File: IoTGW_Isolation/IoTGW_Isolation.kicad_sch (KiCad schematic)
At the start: 17 parts, among them U1 74LVC2G14, U2 HCPL-0600, U3 TLE2426xD, U4 VO2630, U5 TEA1-0505, U6 ISO1452BDWR, U7 PC817, U8 PC817

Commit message: reverse pol prot
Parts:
- added Q?: PMOS, symbol Simulation_SPICE:PMOS
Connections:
- net +5V_OUT: now also Q?.1 (D); no longer C3.1, C5.1, U6.16 (VCC2)
- net GND_OUT: now also Q?.2 (G)
- new net: C3.1, C5.1, U6.16 (VCC2)
- new net +5V_PROT: Q?.3 (S)
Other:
- note added: "choose a pmos will it be ok to use it with rs-485 isolater make a simulation in falstad"

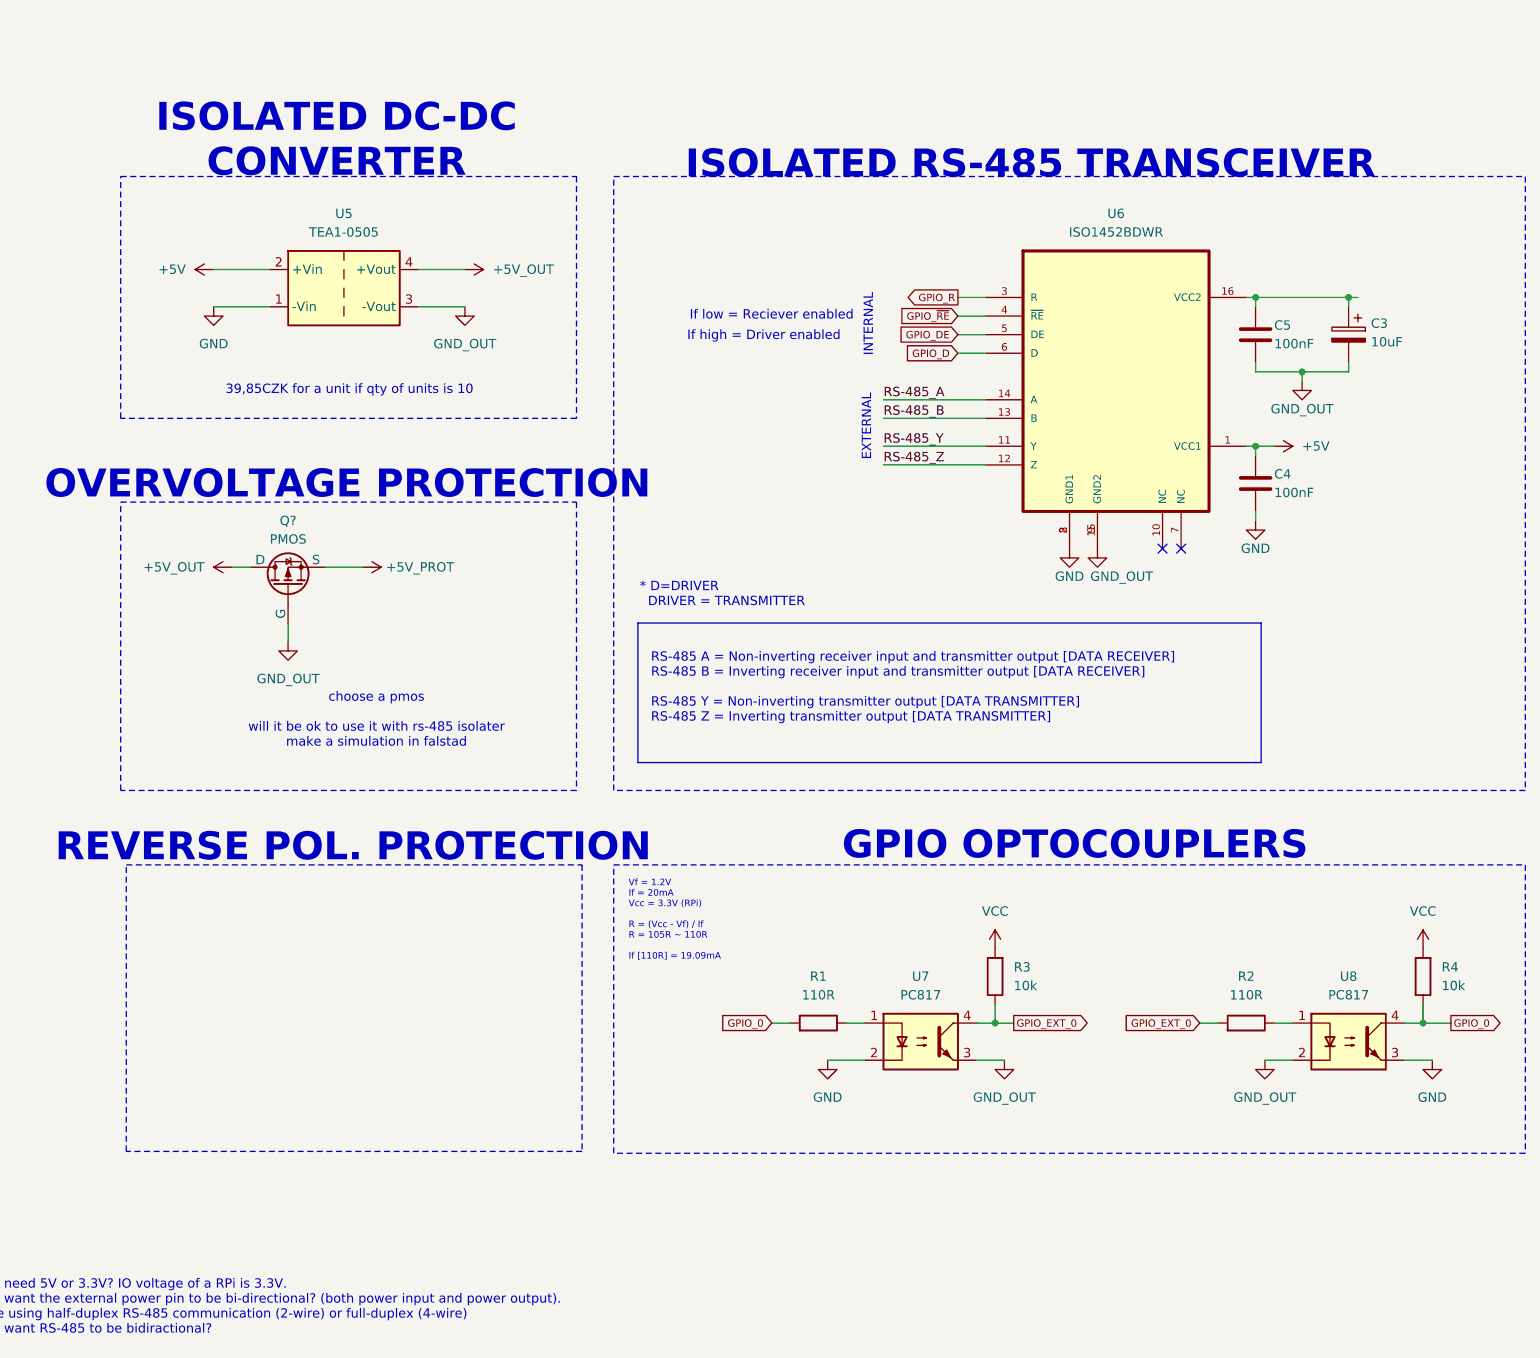
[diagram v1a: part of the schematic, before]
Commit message: updated schematic - comp cost
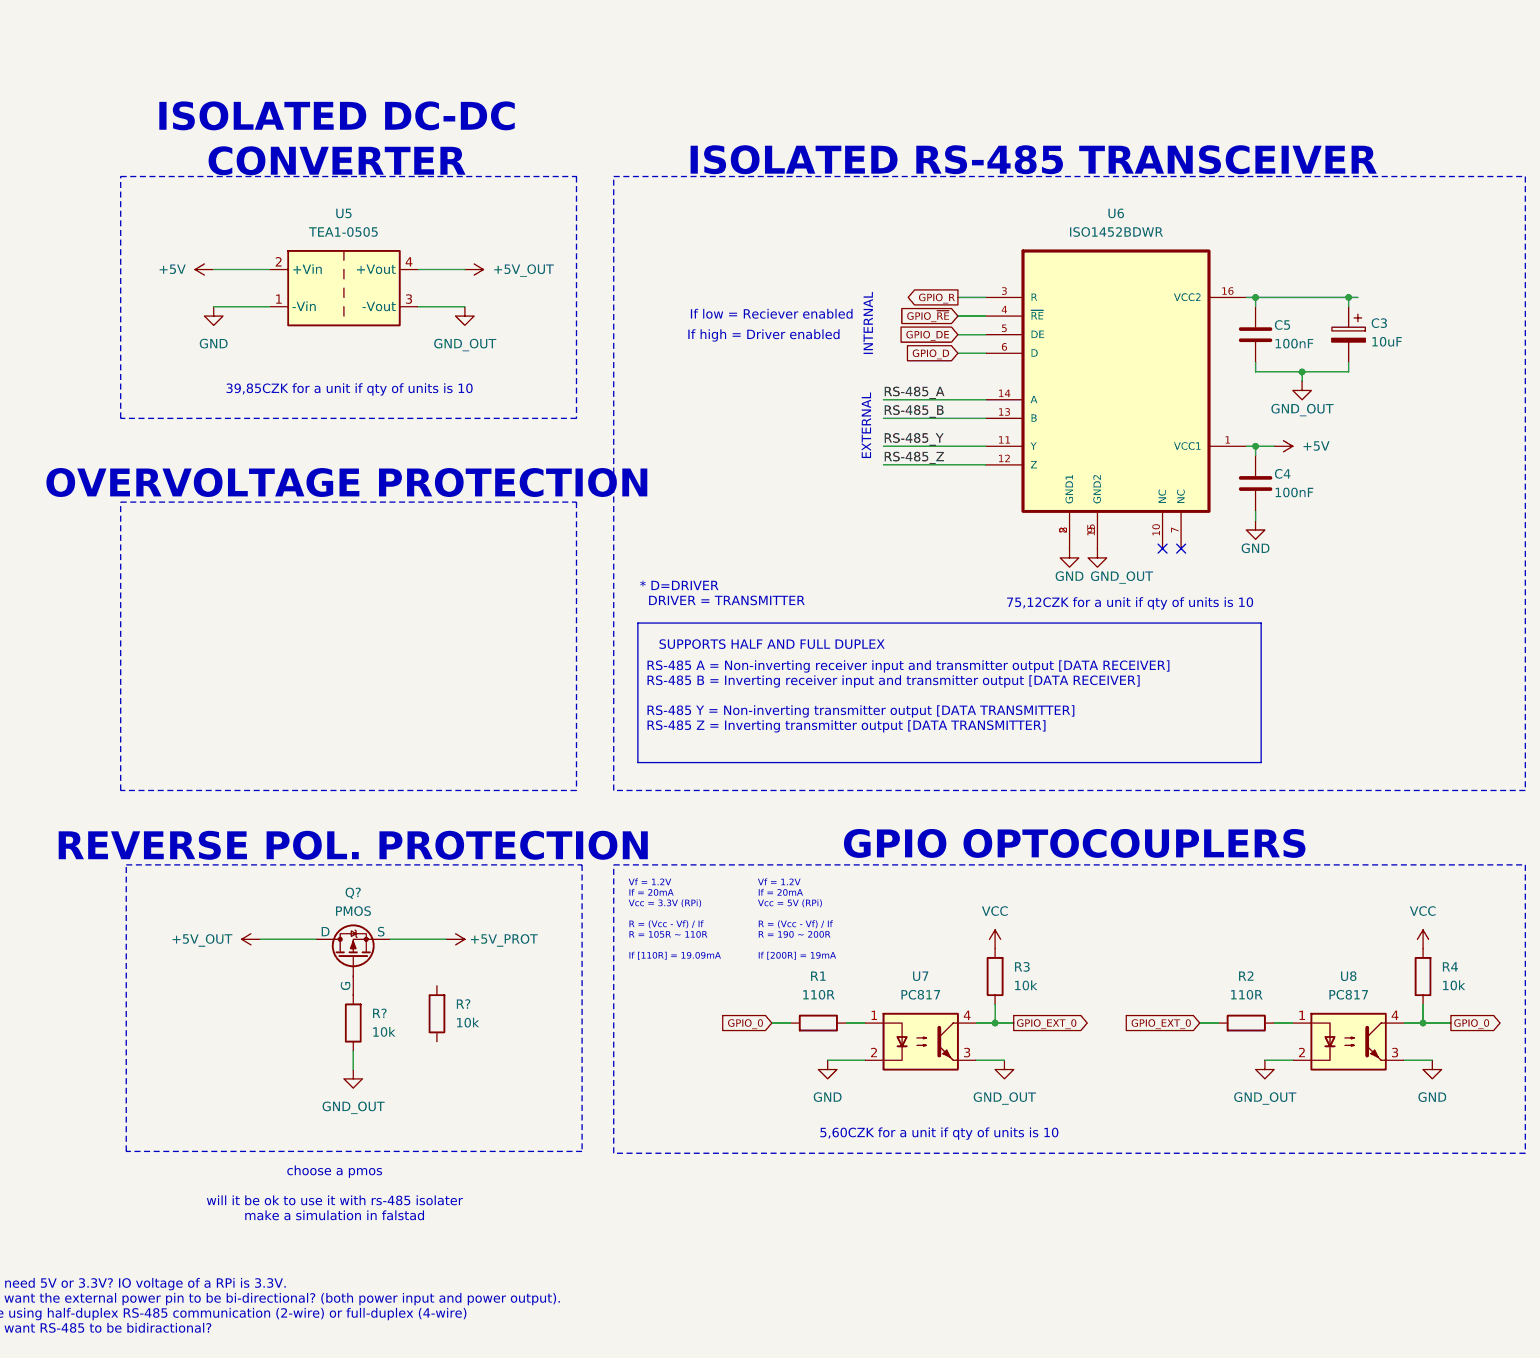
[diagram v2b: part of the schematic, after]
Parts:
- removed Q?: PMOS, symbol Simulation_SPICE:PMOS
- added Q?: PMOS, symbol Simulation_SPICE:PMOS
- added R? (x2): 10k, symbol Device:R
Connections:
- net +5V_OUT: now also Q?.1 (D)
- net +5V_PROT: now also Q?.3 (S)
- net GND_OUT: now also R?.1
- new net: Q?.2 (G), R?.2
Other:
- note added: "5,60CZK for a unit if qty of units is 10"
- note added: "75,12CZK for a unit if qty of units is 10"
- note added: "SUPPORTS HALF AND FULL DUPLEX"
- note added: "Vf = 1.2V If = 20mA Vcc = 5V (RPi) R = (Vcc - Vf) / If R = 190 ~ 200R If [200R] = 19mA"

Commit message: schematic upd
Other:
- note added: "NOT NEEDED SINCE ITS ONLY OUTPUT"
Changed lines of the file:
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@@
+		)
+	)
+	(text "NOT NEEDED SINCE \nITS ONLY OUTPUT"
+		(exclude_from_sim no)
+		(at 77.47 90.805 0)
+		(effects
+			(font
+				(face "Bahnschrift")
+				(size 3 3)
+				(thickness 0.6)
+				(bold yes)
+				(color 0 0 0 1)
+			)
 		)
 	)

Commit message: Schematic update
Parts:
- removed C3: 10uF, symbol Device:C_Polarized
- removed C5: 100nF, symbol Device:C
- removed Q?: PMOS, symbol Simulation_SPICE:PMOS
- removed R? (x2): 10k, symbol Device:R
- removed U6: ISO1452BDWR, ISO1410DWR:SOIC127P1030X265-16N, symbol ISO1410DWR:ISO1452BDWR
- added C3: 100nF, symbol Device:C
- added C5: 10uF, symbol Device:C_Polarized
- added F2: Polyfuse, Fuse:Fuse_0805_2012Metric, symbol Device:Polyfuse
- added H1, H2, H3, H4: M3, symbol Mechanical:MountingHole_Pad
- added J1, J2: JST-XH 2pin, symbol Connector:Conn_01x02_Pin
- added J3: JST-XH 3pin, symbol Connector:Conn_01x03_Pin
- added Q1: Q_PMOS, Package_TO_SOT_SMD:SOT-23-3, symbol Device:Q_PMOS_GSD
- added R1, R10, R12, R14, R8: 10k, symbol Device:R
- added R11, R13, R7, R9: 200R, symbol Device:R
- added R6: 120R, symbol Device:R
- added U10, U11, U12, U9: PC817, Package_DIP:DIP-4_W7.62mm, symbol Isolator:PC817
- added U7: ISO1452BDWR, ISO1410DWR:SOIC127P1030X265-16N, symbol ISO1410DWR:ISO1452BDWR
- R2: renamed from R1; value 110R -> 200R
- R4: renamed from R2; value 110R -> 200R
- renumbered R4 to R5, U7 to U6
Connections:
- net +5V: now also U7.1 (VCC1)
- net +5V_OUT: now also F2.1, Q1.3 (D)
- net +5V_PROT: now also R3.2, R5.2, C3.1, C5.1, Q1.2 (S), R10.2, R12.2, R14.2, R8.2, U7.16 (VCC2)
- net GND: now also U10.3, U11.2, U12.3, U7.2 (GND1), U7.8 (GND1), U9.2
- net GND_OUT: now also C3.2, C5.2, J1.2 (Pin_2), R1.1, U10.2, U11.3, U12.2, U7.15 (GND2), U7.9 (GND2), U9.3
- net GPIO_D: now also U7.6 (D)
- net GPIO_DE: now also U7.5 (DE)
- net GPIO_EXT_0: now also J3.1 (Pin_1)
- net GPIO_R: now also U7.3 (R)
- net GPIO_~{RE}: now also U7.4 (~{RE})
- net RS-485_A: now also J2.1 (Pin_1), R6.2, U7.14 (A)
- net RS-485_B: now also J2.2 (Pin_2), R6.1, U7.13 (B)
- net RS-485_Y: now also U7.11 (Y)
- net RS-485_Z: now also U7.12 (Z)
- net VCC: no longer R3.2, R5.2
- net GPIO_0 renamed GPIO_OPTO_0
- new net: R11.1, U11.1
- new net: Q1.1 (G), R1.2
- new net: R7.1, U9.1
- new net: R13.1, U12.1
- new net: R9.1, U10.1
- new net 5V_CONN: F2.2, J1.1 (Pin_1)
- new net GPIO_EXT_1: J3.2 (Pin_2), R8.1, R9.2, U9.4
- new net GPIO_EXT_2: J3.3 (Pin_3), R12.1, R13.2, U11.4
- new net GPIO_OPTO_1: R10.1, R7.2, U10.4
- new net GPIO_OPTO_2: R11.2, R14.1, U12.4
- no-connect marks 2 -> 8
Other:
- note added: "* D = DRIVER DRIVER = TRANSMITTER"
- note added: "*The unit price is set for an order quantity of 10 units"
- note added: "1. Q: [] 2. Q: [] 3. Q: [] 4. Q: [] 5. Q: []"
- note added: "39,85CZK"
- note added: "5,60CZK"
- note added: "75,12CZK"
- note added: "A zener diode can protect against overvoltage"
- note added: "CIRCUIT PROTECTION"
- note added: "I think we dont need it at all: Cost inneffective."
- note added: "MECHANICAL"
- note added: "SHORT CIRCUIT PROTECTION"
- note added: "low Rds on"
- note removed: "* D=DRIVER DRIVER = TRANSMITTER"
- note removed: "1. Q: Do we need 5V or 3.3V? IO voltage of a RPi is 3.3V. 2. Q: Do we want the external power pin to be bi-directional? (both power input and power output). 3. Q: Are we using half-duplex RS-485 communication (2-wire) or full-duplex (4-wire) 4. Q: Do we want RS-485 to be bidiractional? 5. Q: []"
- note removed: "39,85CZK for a unit if qty of units is 10"
- note removed: "5,60CZK for a unit if qty of units is 10"
- note removed: "75,12CZK for a unit if qty of units is 10"
- note removed: "ISOLATED DC-DC CONVERTER"
- note removed: "NOT NEEDED SINCE ITS ONLY OUTPUT"
- note removed: "OVERVOLTAGE PROTECTION"
- note removed: "choose a pmos will it be ok to use it with rs-485 isolater make a simulation in falstad"
- moved on the sheet: C1, C2, R2, R3, R4, R5, U1A, U1B, U1C, U2, U3, U4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

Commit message: footprints + pcb
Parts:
- removed C1: 220uF, symbol Device:C_Polarized
- removed C2: 1uF, symbol Device:C
- removed J1, J2: JST-XH 2pin, symbol Connector:Conn_01x02_Pin
- removed J3: JST-XH 3pin, symbol Connector:Conn_01x03_Pin
- removed U1: 74LVC2G14, symbol 74xGxx:74LVC2G14
- removed U10, U11, U12, U6, U8, U9: PC817, Package_DIP:DIP-4_W7.62mm, symbol Isolator:PC817
- removed U2: HCPL-0600, Package_SO:SOIC-8_3.9x4.9mm_P1.27mm, symbol Isolator:HCPL-0600
- removed U3: TLE2426xD, Package_SO:SOIC-8_3.9x4.9mm_P1.27mm, symbol Reference_Voltage:TLE2426xD
- removed U4: VO2630, Package_DIP:DIP-8_W7.62mm, symbol Isolator:VO2630
- added J1: Molex 39502-1002, IoTGW:Molex_2pin_3.50, symbol Connector:Conn_01x02_Socket
- added J3: Molex 39502-1007, IoTGW:Molex_7pin_3.50, symbol Connector:Conn_01x07_Socket
- added U3, U4, U5, U6, U7, U8: LTV-817S, Package_DIP:SMDIP-4_W9.53mm, symbol Isolator:LTV-817S
- C1: renamed from C3; footprint (none) -> Capacitor_SMD:C_0805_2012Metric_Pad1.18x1.45mm_HandSolder
- C2: renamed from C4; footprint (none) -> Capacitor_SMD:C_0805_2012Metric_Pad1.18x1.45mm_HandSolder
- C3: renamed from C5; footprint (none) -> Capacitor_Tantalum_SMD:CP_EIA-3216-18_Kemet-A_Pad1.58x1.35mm_HandSolder
- H1, H2, H3, H4: footprint (none) -> MountingHole:MountingHole_3.2mm_M3_Pad_Via
- Q1: footprint Package_TO_SOT_SMD:SOT-23-3 -> (none)
- R10: renamed from R9; footprint (none) -> Resistor_SMD:R_0805_2012Metric_Pad1.20x1.40mm_HandSolder
- R11: renamed from R13; footprint (none) -> Resistor_SMD:R_0805_2012Metric_Pad1.20x1.40mm_HandSolder
- R12: renamed from R5; footprint (none) -> Resistor_SMD:R_0805_2012Metric_Pad1.20x1.40mm_HandSolder
- R13: renamed from R10; footprint (none) -> Resistor_SMD:R_0805_2012Metric_Pad1.20x1.40mm_HandSolder
- R14: footprint (none) -> Resistor_SMD:R_0805_2012Metric_Pad1.20x1.40mm_HandSolder
- R2: renamed from R6; footprint (none) -> Resistor_SMD:R_0805_2012Metric_Pad1.20x1.40mm_HandSolder
- R3: renamed from R2; footprint (none) -> Resistor_SMD:R_0805_2012Metric_Pad1.20x1.40mm_HandSolder
- R4: renamed from R7; footprint (none) -> Resistor_SMD:R_0805_2012Metric_Pad1.20x1.40mm_HandSolder
- R5: renamed from R11; footprint (none) -> Resistor_SMD:R_0805_2012Metric_Pad1.20x1.40mm_HandSolder
- R6: renamed from R3; footprint (none) -> Resistor_SMD:R_0805_2012Metric_Pad1.20x1.40mm_HandSolder
- R7: renamed from R8; footprint (none) -> Resistor_SMD:R_0805_2012Metric_Pad1.20x1.40mm_HandSolder
- R8: renamed from R12; footprint (none) -> Resistor_SMD:R_0805_2012Metric_Pad1.20x1.40mm_HandSolder
- R9: renamed from R4; footprint (none) -> Resistor_SMD:R_0805_2012Metric_Pad1.20x1.40mm_HandSolder
- U2: renamed from U7; footprint ISO1410DWR:SOIC127P1030X265-16N -> Package_SO:SOIC-16W_7.5x10.3mm_P1.27mm
- renumbered F2 to F1, U5 to U1
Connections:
- net +5V: now also J1.2 (Pin_2)
- net 5V_CONN: now also J3.2 (Pin_2)
- net GND: now also J1.1 (Pin_1), U3.2, U4.2, U5.2, U6.3, U7.3, U8.3
- net GND_OUT: now also J3.1 (Pin_1), U3.3, U4.3, U5.3, U6.2, U7.2, U8.2
- net GPIO_EXT_0: now also J3.3 (Pin_3), U3.4
- net GPIO_EXT_1: now also J3.4 (Pin_4), U4.4
- net GPIO_EXT_2: now also J3.5 (Pin_5), U5.4
- net GPIO_OPTO_0: now also U6.4
- net GPIO_OPTO_1: now also U7.4
- net GPIO_OPTO_2: now also U8.4
- net RS-485_A: now also J3.6 (Pin_6)
- net RS-485_B: now also J3.7 (Pin_7)
- net at R5.1: now also U5.1
- net at R9.1: now also U6.1
- net at R4.1: now also U4.1
- net at R11.1: now also U8.1
- net at R10.1: now also U7.1
- net at R3.1: now also U3.1
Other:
- note added: "1. Q: RS-485 to UART bridge 2. Q: Better connectors Molex terminals 3. Q: Is there a need for cooling? - Fuse, ISO, etc 4. Q: PCB Layout 5. Q: []"
- note added: "15,71CZK"
- note added: "5,49CZK"
- note removed: "1. Q: [] 2. Q: [] 3. Q: [] 4. Q: [] 5. Q: []"
- note removed: "40mA MAX - TOO LITTLE - HIGH COST"
- note removed: "5,60CZK"
- note removed: "PS9121-F3-AX is 15Mb/s single ch"
- note removed: "SHORT CIRCUIT PROTECTION"
- note removed: "TLP2270(TP4,E is 20Mb/s cost, for 10 units is 43,35CZK"
- note removed: "VO0661T is 10Mb/s, cost for 10 units is 59,39CZK"
- note removed: "VO2630 is 10Mb/s, cost for 10 units is 38,34CZK"
- moved on the sheet: H1, H2, H3, H4

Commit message: PCB update, connectors 8pin
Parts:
- removed J1: Molex 39502-1002, IoTGW:Molex_2pin_3.50, symbol Connector:Conn_01x02_Socket
- removed J3: Molex 39502-1007, IoTGW:Molex_7pin_3.50, symbol Connector:Conn_01x07_Socket
- added J4, J5: 39502-1008, IoTGW:Molex_8pin_3.50, symbol Connector:Conn_01x08_Socket
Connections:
- net GPIO_~{RE} is gone; now on net GPIO_COMM: U2.4 (~{RE})
- net +5V: now also J4.1 (Pin_1)
- net 5V_CONN: now also J5.1 (Pin_1)
- net GND: now also J4.2 (Pin_2)
- net GND_OUT: now also J5.2 (Pin_2)
- net GPIO_D: now also J4.8 (Pin_8)
- net GPIO_EXT_0: now also J5.3 (Pin_3)
- net GPIO_EXT_1: now also J5.4 (Pin_4)
- net GPIO_EXT_2: now also J5.5 (Pin_5)
- net GPIO_OPTO_0: now also J4.3 (Pin_3)
- net GPIO_OPTO_1: now also J4.4 (Pin_4)
- net GPIO_OPTO_2: now also J4.5 (Pin_5)
- net GPIO_R: now also J4.7 (Pin_7)
- net RS-485_A: now also J5.6 (Pin_6)
- net RS-485_B: now also J5.7 (Pin_7)
- net GPIO_DE renamed GPIO_COMM
- net GPIO_COMM: now also J4.6 (Pin_6)
- no-connect marks 8 -> 9
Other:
- note added: "1. Q: Does the RS-485 have to be on its own separeted connector (twisted pair) 2. Q: Are RPi GPIOs 5V safe, requires confirmation. 3. Q: 4. Q: 5. Q: []"
- note added: "1. Q: Output and Input connectors 2. Q: Better connectors Molex terminals 3. Q: Is there a need for cooling? - Fuse, ISO, etc 4. Q: PCB Layout 5. Q: []"
- note added: "34,83CZK"
- note added: "36,84CZK"
- note added: "F"
- note added: "If we want half-duplex we are going to use one gpio"
- note added: "M"
- note added: "RX"
- note added: "TX"
- note removed: "1. Q: RS-485 to UART bridge 2. Q: Better connectors Molex terminals 3. Q: Is there a need for cooling? - Fuse, ISO, etc 4. Q: PCB Layout 5. Q: []"
- moved on the sheet: H1, H2, H3, H4

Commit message: PCB update
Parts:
- removed J5: 39502-1008, IoTGW:Molex_8pin_3.50, symbol Connector:Conn_01x08_Socket
- added J1: 39502-1008, IoTGW:Molex_8pin_3.50, symbol Connector:Conn_01x08_Socket
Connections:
- net +5V: now also R12.2, R13.2, R14.2
- net +5V_OUT: now also C1.1, C3.1, R6.2, R7.2, R8.2, U2.16 (VCC2)
- net +5V_PROT: no longer C1.1, C3.1, R12.2, R13.2, R14.2, R6.2, R7.2, R8.2, U2.16 (VCC2)
- net 5V_CONN: now also J1.8 (Pin_8)
- net GND_OUT: now also J1.7 (Pin_7)
- net GPIO_EXT_0: now also J1.6 (Pin_6)
- net GPIO_EXT_1: now also J1.5 (Pin_5)
- net GPIO_EXT_2: now also J1.4 (Pin_4)
- net RS-485_A: now also J1.3 (Pin_3)
- net RS-485_B: now also J1.2 (Pin_2)
